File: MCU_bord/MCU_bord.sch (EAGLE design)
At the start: 19 parts

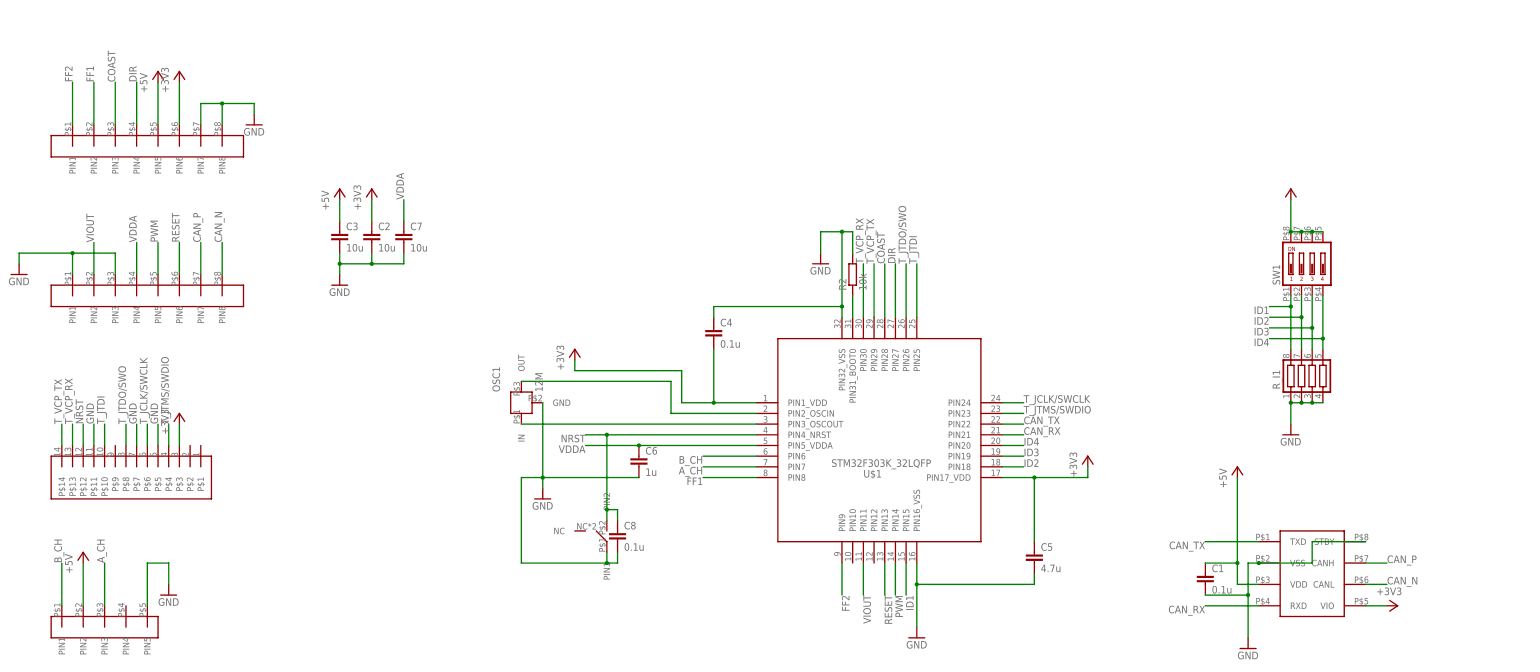
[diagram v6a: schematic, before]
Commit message: canトランシーバ終端抵抗追加、電源確認用LED追加
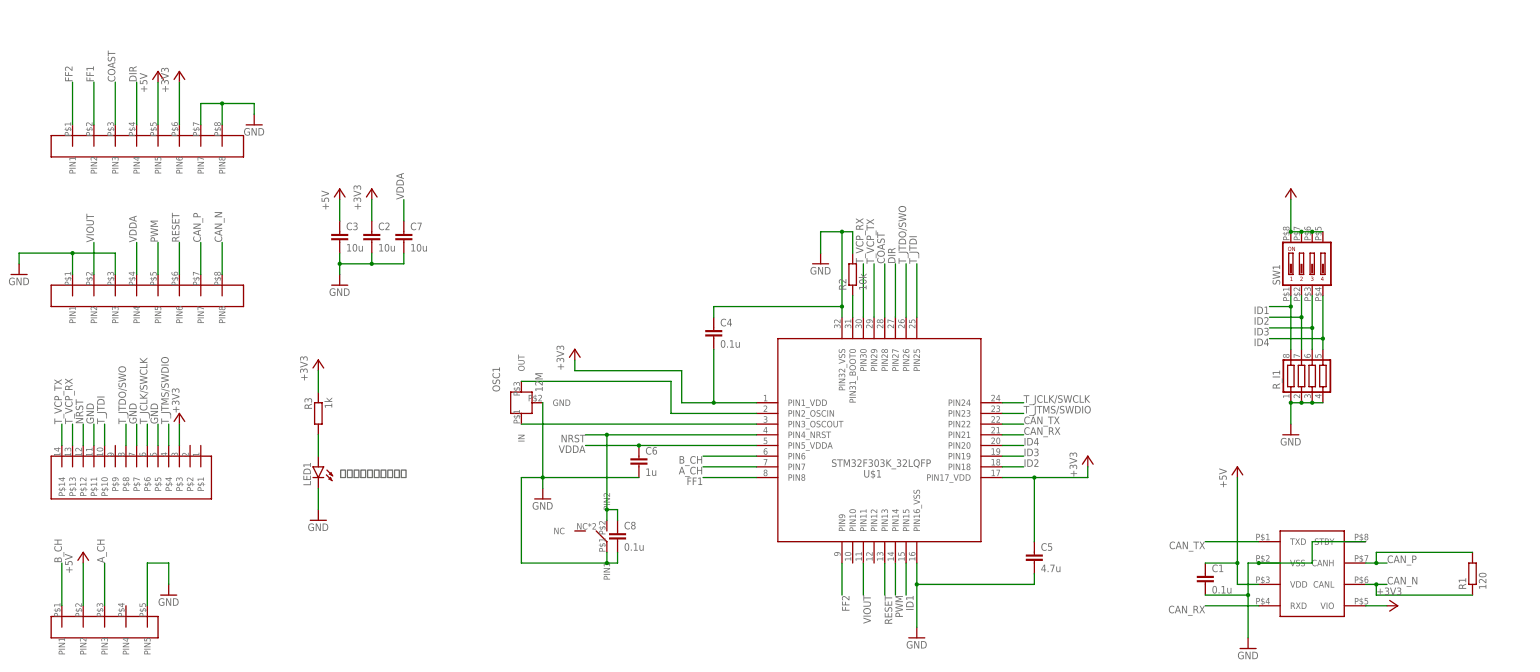
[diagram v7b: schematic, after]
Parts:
- added LED1: (no value), user_leds:1608LED
- added R1: 120, user_rcl:R_REG
- added R3: 1k, user_rcl:R_REG
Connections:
- new net N$4: LED1.A, R3.2
- net +3V3: now also R3.1
- net CAN_N: now also R1.1
- net CAN_P: now also R1.2
- net GND: now also LED1.K
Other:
- note added: "電源確認用色指定なし"
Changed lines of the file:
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@@
 <part name="+3V7" library="supply1" library_urn="urn:adsk.eagle:library:371" deviceset="+3V3" device=""/>
 <part name="CON3" library="user_conector" deviceset="XH_5P" device=""/>
+<part name="R1" library="user_rcl" deviceset="R_REG" device="" value="120"/>
+<part name="LED1" library="user_leds" deviceset="1608LED" device=""/>
+<part name="R3" library="user_rcl" deviceset="R_REG" device="" value="1k"/>
+<part name="GND10" library="supply1" library_urn="urn:adsk.eagle:library:371" deviceset="GND" device=""/>
+<part name="+3V8" library="supply1" library_urn="urn:adsk.eagle:library:371" deviceset="+3V3" device=""/>
 </parts>
 <sheets>
 <sheet>
 <plain>
+<text x="-45.72" y="43.18" size="1.778" layer="97">電源確認用色指定なし</text>
 </plain>
 <instances>
@@
 <instance part="+3V6" gate="G$1" x="180.34" y="111.76" smashed="yes"/>
 <instance part="+3V7" gate="G$1" x="-83.82" y="58.42" smashed="yes">
-<attribute name="VALUE" x="-86.36" y="53.34" size="1.778" layer="96" rot="R90"/>
+<attribute name="VALUE" x="-83.82" y="58.42" size="1.778" layer="96" rot="R90"/>
 </instance>
 <instance part="CON3" gate="G$1" x="-101.6" y="7.62" smashed="yes"/>
+<instance part="R1" gate="G$1" x="223.52" y="20.32" smashed="yes" rot="R90">
+<attribute name="NAME" x="222.0214" y="16.51" size="1.778" layer="95" rot="R90"/>
+<attribute name="VALUE" x="226.822" y="16.51" size="1.778" layer="96" rot="R90"/>
+</instance>
+<instance part="LED1" gate="G$1" x="-50.8" y="45.72" smashed="yes" rot="MR0">
+<attribute name="NAME" x="-54.356" y="41.148" size="1.778" layer="95" rot="MR90"/>
+<attribute name="VALUE" x="-56.515" y="41.148" size="1.778" layer="96" rot="MR90"/>
+</instance>
+<instance part="R3" gate="G$1" x="-50.8" y="58.42" smashed="yes" rot="MR270">
+<attribute name="NAME" x="-52.2986" y="62.23" size="1.778" layer="95" rot="MR270"/>
+<attribute name="VALUE" x="-47.498" y="62.23" size="1.778" layer="96" rot="MR270"/>
+</instance>
+<instance part="GND10" gate="1" x="-50.8" y="33.02" smashed="yes">
+<attribute name="VALUE" x="-53.34" y="30.48" size="1.778" layer="96"/>
+</instance>
+<instance part="+3V8" gate="G$1" x="-50.8" y="71.12" smashed="yes">
+<attribute name="VALUE" x="-53.34" y="66.04" size="1.778" layer="96" rot="R90"/>
+</instance>
 </instances>
 <busses>
@@
 <segment>
 <pinref part="IC1" gate="G$1" pin="CANH"/>
-<wire x1="198.12" y1="22.86" x2="203.2" y2="22.86" width="0.1524" layer="91"/>
+<wire x1="198.12" y1="22.86" x2="200.66" y2="22.86" width="0.1524" layer="91"/>
 <label x="203.2" y="22.86" size="1.778" layer="95"/>
+<pinref part="R1" gate="G$1" pin="2"/>
+<wire x1="200.66" y1="22.86" x2="203.2" y2="22.86" width="0.1524" layer="91"/>
+<wire x1="223.52" y1="25.4" x2="200.66" y2="25.4" width="0.1524" layer="91"/>
+<wire x1="200.66" y1="25.4" x2="200.66" y2="22.86" width="0.1524" layer="91"/>
+<junction x="200.66" y="22.86"/>
 </segment>
 </net>
@@
 <segment>
 <pinref part="IC1" gate="G$1" pin="CANL"/>
-<wire x1="198.12" y1="17.78" x2="203.2" y2="17.78" width="0.1524" layer="91"/>
+<wire x1="198.12" y1="17.78" x2="200.66" y2="17.78" width="0.1524" layer="91"/>
 <label x="203.2" y="17.78" size="1.778" layer="95"/>
+<wire x1="200.66" y1="17.78" x2="203.2" y2="17.78" width="0.1524" layer="91"/>
+<wire x1="200.66" y1="17.78" x2="200.66" y2="15.24" width="0.1524" layer="91"/>
+<junction x="200.66" y="17.78"/>
+<pinref part="R1" gate="G$1" pin="1"/>
+<wire x1="200.66" y1="15.24" x2="223.52" y2="15.24" width="0.1524" layer="91"/>
 </segment>
 </net>
@@
 <junction x="180.34" y="60.96"/>
 </segment>
+<segment>
+<pinref part="LED1" gate="G$1" pin="K"/>
+<pinref part="GND10" gate="1" pin="GND"/>
+<wire x1="-50.8" y1="40.64" x2="-50.8" y2="35.56" width="0.1524" layer="91"/>
+</segment>
 </net>
 <net name="+5V" class="0">
@@
 <junction x="185.42" y="101.6"/>
 </segment>
+<segment>
+<pinref part="+3V8" gate="G$1" pin="+3V3"/>
+<pinref part="R3" gate="G$1" pin="1"/>
+<wire x1="-50.8" y1="68.58" x2="-50.8" y2="63.5" width="0.1524" layer="91"/>
+</segment>
 </net>
 <net name="CAN_TX" class="0">
@@
 </segment>
 </net>
+<net name="N$4" class="0">
+<segment>
+<pinref part="R3" gate="G$1" pin="2"/>
+<pinref part="LED1" gate="G$1" pin="A"/>
+<wire x1="-50.8" y1="53.34" x2="-50.8" y2="48.26" width="0.1524" layer="91"/>
+</segment>
+</net>
